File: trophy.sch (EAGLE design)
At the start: 14 parts, among them J1 AVR_SPI_PROG_3X2PTH, U1 ATTINY85SOIC8

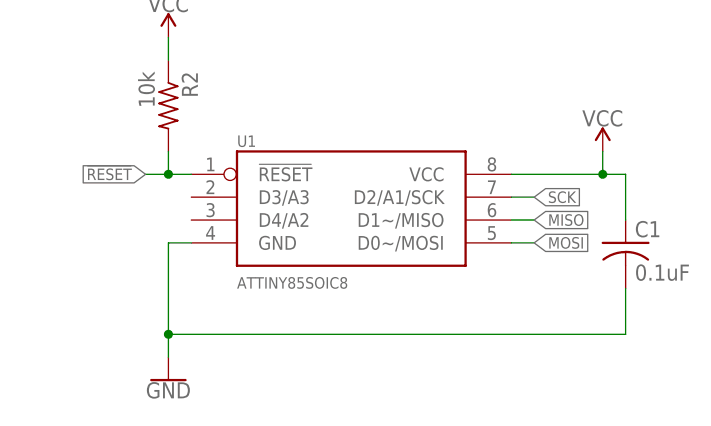
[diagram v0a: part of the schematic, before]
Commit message: Round corners and make final tweaks for trophy
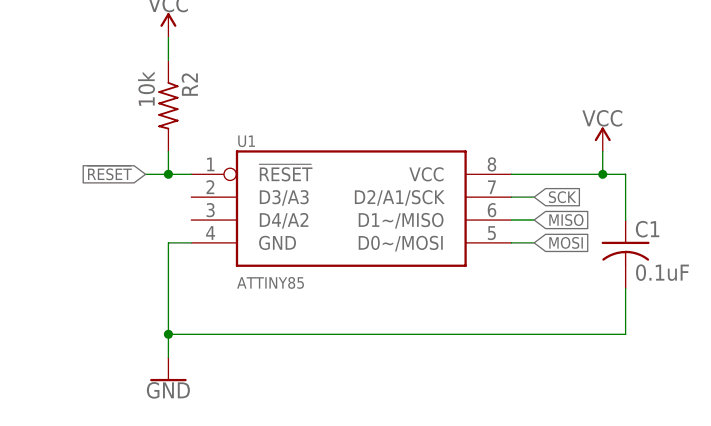
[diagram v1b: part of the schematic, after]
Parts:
- U1: value ATTINY85SOIC8 -> ATTINY85; device JoshCustom:ATTINY85SOIC8 -> JoshCustom:ATTINY85
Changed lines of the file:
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@@
 </classes>
 <parts>
-<part name="U1" library="JoshCustom" deviceset="ATTINY85" device="SOIC8"/>
+<part name="U1" library="JoshCustom" deviceset="ATTINY85" device="" value="ATTINY85"/>
 <part name="LED1" library="RoboJackets-LEDs" deviceset="WS2812B" device=""/>
 <part name="LED2" library="RoboJackets-LEDs" deviceset="WS2812B" device=""/>
